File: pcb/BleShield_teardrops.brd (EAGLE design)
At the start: 23 parts, among them U1 ARDUINO_SHIELDNOHOLES, Y1 32.768KHz, 10 PPM

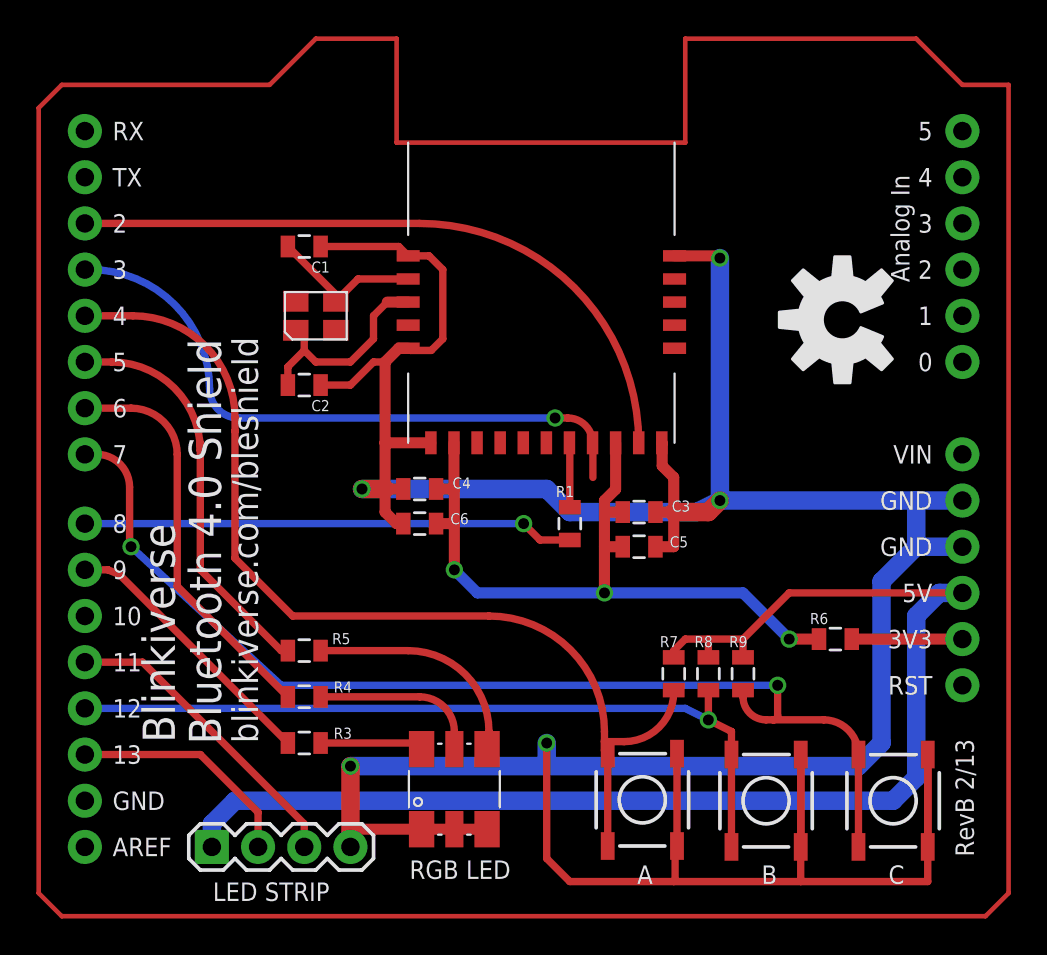
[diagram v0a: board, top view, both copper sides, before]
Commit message: fixed silkscreens, minor re-routing, added teardrops
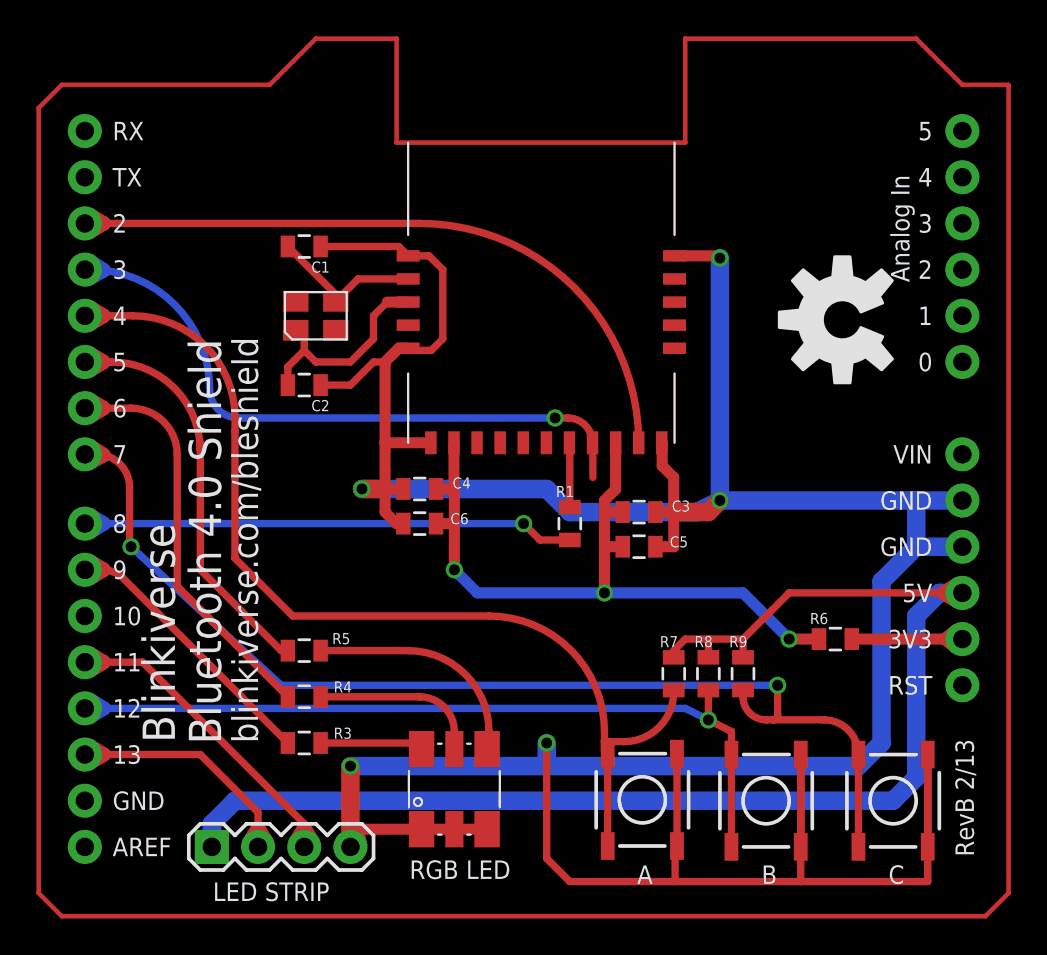
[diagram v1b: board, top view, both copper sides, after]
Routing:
- net SCK: track 12.7 -> 18.3 mm
- net MOSI: track 17.0 -> 22.6 mm
- net 3.3V: track 6.08 -> 8.94 mm
- net TX: track 33.8 -> 36.6 mm
- net SWITCH_C: track 60.2 -> 63.0 mm
- net GND: track 212.8 -> 215.6 mm
- net SWITCH_A: track 54.0 -> 56.8 mm
- net LED_RED: track 22.0 -> 24.8 mm
- net LED_BLUE: track 15.1 -> 17.8 mm
- net RESET: track 27.0 -> 29.8 mm
- net LED_GREEN: track 22.0 -> 24.8 mm
- net SWITCH_B: track 43.8 -> 46.6 mm
- net RX: track 35.5 -> 38.3 mm
- net 5V: track 72.6 -> 75.4 mm
